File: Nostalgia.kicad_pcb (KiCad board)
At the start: 2 copper layers, 70 x 102 mm, 46 parts, among them J10 490107670612, J20 USB-C6, K85 Val, U30 1117-3.3, U40 ESP32-S3-WROOM-1-N16R8

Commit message: WIP
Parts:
- U40: moved to B.Cu
- turned U40 to 180 degrees

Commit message: WIP
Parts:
- added REF**: TACT_6x6_SMD, _custom:TACT_6x6_SMD, F.Cu at (18.0, -41.2)
- added REF**: TACT_6x6_SMD, _custom:TACT_6x6_SMD, F.Cu at (52.0, -41.2)
- added REF**: TACT_6x6_SMD, _custom:TACT_6x6_SMD, F.Cu at (35.0, -45.2)
- added REF**: TACT_6x6_SMD, _custom:TACT_6x6_SMD, F.Cu at (35.0, -37.2)
- moved K85 81.0 mm to (99.0, -48.0)
- moved K85 59.5 mm to (94.0, -41.0)
- moved K85 57.1 mm to (109.0, -48.0)
- moved K85 44.0 mm to (95.4, -56.0)
- moved K85 5.00 mm to (35.0, -29.0)
- moved K85 5.00 mm to (18.0, -29.0)
- moved K85 5.00 mm to (52.0, -29.0)
- moved K85 4.00 mm to (18.0, -22.0)
- moved K85 4.00 mm to (35.0, -22.0)
- moved K85 4.00 mm to (52.0, -22.0)
- moved K85 3.00 mm to (18.0, -15.0)
- moved K85 3.00 mm to (52.0, -15.0)
- moved K85 3.00 mm to (35.0, -15.0)
- moved K85 2.00 mm to (35.0, -8.00)
- moved K85 2.00 mm to (18.0, -8.00)
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
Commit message: Schemat
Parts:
- removed BT60 (x3): 18650, _custom:Bat_BHC-18650-1P
- removed K85 (x16): Val, _custom:TACT_6x3.5_SMD
- removed the REF** at (18.0, -41.2)
- removed the REF** at (52.0, -41.2)
- removed the REF** at (35.0, -45.2)
- removed the REF** at (35.0, -37.2)
- added BAT1: 18650, _custom:Bat_BH-18650-A1AJ005, B.Cu at (12.0, -38.2)
- added BAT2: 18650, _custom:Bat_BH-18650-A1AJ005, B.Cu at (35.0, -38.2)
- added BAT3: 18650, _custom:Bat_BH-18650-A1AJ005, B.Cu at (58.0, -38.2)
- added C1: 10u, _custom:C_0603, F.Cu at (123.2, -12.3)
- added C2: 10u, _custom:C_0603, F.Cu at (107.6, -7.67)
- added D1: LED, _custom:LED_0805, F.Cu at (108.1, -12.2)
- added D2: LED, _custom:LED_0805, F.Cu at (108.1, -9.85)
- added K1: TACT_6x3_SMD, _custom:TACT_6x3_SMD, F.Cu at (18.0, -29.0)
- added K10: TACT_6x3_SMD, _custom:TACT_6x3_SMD, F.Cu at (18.0, -8.00)
- added K11: TACT_6x3_SMD, _custom:TACT_6x3_SMD, F.Cu at (35.0, -8.00)
- added K12: TACT_6x3_SMD, _custom:TACT_6x3_SMD, F.Cu at (52.0, -8.00)
- added K13: TACT_6x6_SMD, _custom:TACT_6x6_SMD, F.Cu at (18.0, -41.2)
- added K14: TACT_6x6_SMD, _custom:TACT_6x6_SMD, F.Cu at (35.0, -45.2)
- added K15: TACT_6x6_SMD, _custom:TACT_6x6_SMD, F.Cu at (35.0, -37.2)
- added K16: TACT_6x6_SMD, _custom:TACT_6x6_SMD, F.Cu at (52.0, -41.2)
- added K2: TACT_6x3_SMD, _custom:TACT_6x3_SMD, F.Cu at (35.0, -29.0)
- added K3: TACT_6x3_SMD, _custom:TACT_6x3_SMD, F.Cu at (52.0, -29.0)
- added K4: TACT_6x3_SMD, _custom:TACT_6x3_SMD, F.Cu at (18.0, -22.0)
- added K5: TACT_6x3_SMD, _custom:TACT_6x3_SMD, F.Cu at (35.0, -22.0)
- added K6: TACT_6x3_SMD, _custom:TACT_6x3_SMD, F.Cu at (52.0, -22.0)
- added K7: TACT_6x3_SMD, _custom:TACT_6x3_SMD, F.Cu at (18.0, -15.0)
- added K8: TACT_6x3_SMD, _custom:TACT_6x3_SMD, F.Cu at (35.0, -15.2)
- added K9: TACT_6x3_SMD, _custom:TACT_6x3_SMD, F.Cu at (52.0, -15.2)
- added R1: 1k, _custom:R_0603, F.Cu at (123.2, -10.3)
- added R2: 1k, _custom:R_0603, F.Cu at (123.2, -8.38)
- added R3: 1k2, _custom:R_0603, F.Cu at (123.2, -6.42)
- added TP2: Chg, _custom:Testpoint_2.00mm, F.Cu at (117.2, -2.90)
- added TP5: Stby, _custom:Testpoint_2.00mm, F.Cu at (117.2, 0.66)
- added U1: TP4056, _custom:SO8-PowerPad, F.Cu at (118.7, -8.96)
- J10, J20: moved to B.Cu
- moved J20 104.0 mm to (70.0, -82.2)
- moved J10 86.3 mm to (56.5, -99.0), turned to 180 degrees
- moved U40 5.50 mm to (35.4, -95.2)
- moved REF** 2.00 mm to (35.0, -78.0)
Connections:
- J20 pad A9: 5V -> VUSB
- J20 pad B9: 5V -> VUSB
- U40 pad 36: unconnected-(U40-Rx0/IO44-Pad36) -> /Debug-Rx
- U40 pad 37: unconnected-(U40-Tx0/IO43-Pad37) -> /Debug-Tx

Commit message: WIP
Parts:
- added C10: 100n, _custom:C_0603, F.Cu at (125.7, 3.37)
- added C4: 10u, _custom:C_0603, F.Cu at (125.7, -0.53)
- added C5: 10u, _custom:C_0603, F.Cu at (125.7, 1.42)
- added U5: TPS613222ADBV, _custom:SOT23-5, F.Cu at (129.3, 0.56)

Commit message: WIP
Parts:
- removed C30, C32: 10u, _custom:C_0603
- removed C31, C33: 1u, _custom:C_0603
- removed FID1, FID2, FID3, FID4, FID5, FID6: 1.00mm, _custom:Fiducial_1.00mm
- removed REF**: OLED_2.42inch_board, _custom:OLED_2.42inch_board
- removed TP2: Chg, _custom:Testpoint_2.00mm
- removed TP5: Stby, _custom:Testpoint_2.00mm
- removed U30: 1117-3.3, _custom:SOT223
- added C3: 10u, _custom:C_0603, F.Cu at (60.6, 9.25)
- added C6: 10u, _custom:C_0603, F.Cu at (60.6, 11.2)
- added C7: 100n, _custom:C_0603, F.Cu at (60.6, 13.2)
- added C8: 10u, _custom:C_0603, F.Cu at (60.6, 15.1)
- added DISP1: OLED, _custom:OLED_2.42inch_board, F.Cu at (35.0, -78.0)
- added L1: 2.2uH, _custom:DJNR3015, F.Cu at (73.5, 12.2)
- added L4: 4.7uH, _custom:DJNR3015, F.Cu at (125.8, 6.50)
- added R4: 1M, _custom:R_0603, F.Cu at (60.6, 17.1)
- added R5: 180k, _custom:R_0603, F.Cu at (60.6, 19.0)
- added R6: 100R, _custom:R_0603, F.Cu at (60.6, 20.9)
- added U2: TPS63000, _custom:Texas_DRC0010J_ThermalVias, F.Cu at (73.3, 17.8)
- C10: value 100n -> 10u
- moved J10 41.4 mm to (15.1, -98.7)
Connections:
- J10 pad 2: 5V -> VUSB
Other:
- board text added: "102"
- board text removed: "70"

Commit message: WIP
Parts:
- removed DISP1: OLED, _custom:OLED_2.42inch_board
- added DISP2: OLED, _custom:OLED_2.42inch_board_2, F.Cu at (35.5, -80.2)
- added R7: 1M, _custom:R_0603, F.Cu at (89.2, 1.00)
- K1, K10, K11, K12, K2, K3, K4, K5, K6, K7, K8, K9: value TACT_6x3_SMD -> CONFIG
- moved BAT1 0.50 mm to (12.5, -38.2)
- moved BAT2 0.50 mm to (35.5, -38.2)
- moved BAT3 0.50 mm to (58.5, -38.2)
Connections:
- K1 pad 1: unconnected-(K1-Pad1) -> /Col0
- K1 pad 2: unconnected-(K1-Pad2) -> /Row0
- K10 pad 1: unconnected-(K10-Pad1) -> /Col0
- K10 pad 2: unconnected-(K10-Pad2) -> /Row3
- K11 pad 1: unconnected-(K11-Pad1) -> /Col1
- K11 pad 2: unconnected-(K11-Pad2) -> /Row3
- K12 pad 1: unconnected-(K12-Pad1) -> /Col2
- K12 pad 2: unconnected-(K12-Pad2) -> /Row3
- K13 pad 1: unconnected-(K13-Pad1) -> /Col3
- K13 pad 2: unconnected-(K13-Pad2) -> /Row2
- K14 pad 1: unconnected-(K14-Pad1) -> /Col3
- K14 pad 2: unconnected-(K14-Pad2) -> /Row0
- K15 pad 1: unconnected-(K15-Pad1) -> /Col3
- K15 pad 2: unconnected-(K15-Pad2) -> /Row1
- K16 pad 1: unconnected-(K16-Pad1) -> /Col3
- K16 pad 2: unconnected-(K16-Pad2) -> /Row3
- K2 pad 1: unconnected-(K2-Pad1) -> /Col1
- K2 pad 2: unconnected-(K2-Pad2) -> /Row0
- K3 pad 1: unconnected-(K3-Pad1) -> /Col2
- K3 pad 2: unconnected-(K3-Pad2) -> /Row0
- K4 pad 1: unconnected-(K4-Pad1) -> /Col0
- K4 pad 2: unconnected-(K4-Pad2) -> /Row1
- K5 pad 1: unconnected-(K5-Pad1) -> /Col1
- K5 pad 2: unconnected-(K5-Pad2) -> /Row1
- K6 pad 1: unconnected-(K6-Pad1) -> /Col2
- K6 pad 2: unconnected-(K6-Pad2) -> /Row1
- K7 pad 1: unconnected-(K7-Pad1) -> /Col0
- K7 pad 2: unconnected-(K7-Pad2) -> /Row2
- K8 pad 1: unconnected-(K8-Pad1) -> /Col1
- K8 pad 2: unconnected-(K8-Pad2) -> /Row2
- K9 pad 1: unconnected-(K9-Pad1) -> /Col2
- K9 pad 2: unconnected-(K9-Pad2) -> /Row2
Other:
- board size 70 x 102 mm -> 71 x 102 mm

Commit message: WIP
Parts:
- moved K16 7.94 mm to (59.0, -45.0)
- moved K12 7.62 mm to (59.0, -11.0)
- moved K3 7.62 mm to (59.0, -32.0)
- moved K6 7.62 mm to (59.0, -25.0)
- moved K9 7.62 mm to (59.0, -18.2)
- moved K13 6.25 mm to (13.0, -45.0)
- moved K1 5.83 mm to (13.0, -32.0)
- moved K10 5.83 mm to (13.0, -11.0)
- moved K4 5.83 mm to (13.0, -25.0)
- moved K7 5.83 mm to (13.0, -18.0)
- moved K14 3.88 mm to (36.0, -49.0)
- moved K15 3.88 mm to (36.0, -41.0)
- moved K11 3.16 mm to (36.0, -11.0)
- moved K2 3.16 mm to (36.0, -32.0)
- moved K5 3.16 mm to (36.0, -25.0)
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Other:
- board size 71 x 102 mm -> 72 x 102 mm
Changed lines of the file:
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@@
 	(footprint "_custom:TACT_6x3_SMD"
 		(layer "F.Cu")
-		(at 35 -8)
+		(at 36 -11)
 		(descr "SMD Pushbutton")
 		(property "Reference" "K11"
@@
 	(footprint "_custom:TACT_6x3_SMD"
 		(layer "F.Cu")
-		(at 52 -22)
+		(at 59 -25)
 		(descr "SMD Pushbutton")
 		(property "Reference" "K6"
@@
 	(footprint "_custom:TACT_6x3_SMD"
 		(layer "F.Cu")
-		(at 35 -15.25)
+		(at 36 -18.25)
 		(descr "SMD Pushbutton")
 		(property "Reference" "K8"
@@
 	(footprint "_custom:TACT_6x6_SMD"
 		(layer "F.Cu")
-		(at 35 -45.25 180)
+		(at 36 -49 180)
 		(descr "C&K Components SPST SMD PTS645 Series 6mm Tact Switch")
 		(tags "SPST Button Switch")
@@
 	(footprint "_custom:TACT_6x3_SMD"
 		(layer "F.Cu")
-		(at 18 -8)
+		(at 13 -11)
 		(descr "SMD Pushbutton")
 		(property "Reference" "K10"
@@
 	(footprint "_custom:TACT_6x3_SMD"
 		(layer "F.Cu")
-		(at 35 -22)
+		(at 36 -25)
 		(descr "SMD Pushbutton")
 		(property "Reference" "K5"
@@
 	(footprint "_custom:TACT_6x3_SMD"
 		(layer "F.Cu")
-		(at 18 -15)
+		(at 13 -18)
 		(descr "SMD Pushbutton")
 		(property "Reference" "K7"
@@
 	(footprint "_custom:TACT_6x6_SMD"
 		(layer "F.Cu")
-		(at 52 -41.25)
+		(at 59 -45)
 		(descr "C&K Components SPST SMD PTS645 Series 6mm Tact Switch")
 		(tags "SPST Button Switch")
@@
 	(footprint "_custom:TACT_6x6_SMD"
 		(layer "F.Cu")
-		(at 35 -37.25)
+		(at 36 -41)
 		(descr "C&K Components SPST SMD PTS645 Series 6mm Tact Switch")
 		(tags "SPST Button Switch")
@@
 	(footprint "_custom:TACT_6x3_SMD"
 		(layer "F.Cu")
-		(at 18 -22)
+		(at 13 -25)
 		(descr "SMD Pushbutton")
 		(property "Reference" "K4"
@@
 	(footprint "_custom:OLED_2.42inch_board_2"
 		(layer "F.Cu")
-		(at 35.5 -80.25)
+		(at 36 -80.25)
 		(property "Reference" "DISP2"
 			(at 0 -0.5 0)
@@
 		)
 		(fp_line
-			(start -31 -19.5)
-			(end -31 19.5)
+			(start -31 -18.8)
+			(end -31 20.2)
 			(stroke
 				(width 0.1)
@@
 		)
 		(fp_line
-			(start -19 19.5)
-			(end -31 19.5)
+			(start -19 20.2)
+			(end -31 20.2)
 			(stroke
 				(width 0.1)
@@
 		)
 		(fp_line
-			(start -19 19.5)
-			(end -18 20.5)
+			(start -19 20.2)
+			(end -18 21.2)
 			(stroke
 				(width 0.1)
@@
 		)
 		(fp_line
-			(start -18 20.5)
-			(end 18 20.5)
+			(start -18 21.2)
+			(end 18 21.2)
 			(stroke
 				(width 0.1)
@@
 		)
 		(fp_line
-			(start 19 19.5)
-			(end 18 20.5)
+			(start 19 20.2)
+			(end 18 21.2)
 			(stroke
 				(width 0.1)
@@
 		)
 		(fp_line
-			(start 31 -19.5)
-			(end -31 -19.5)
+			(start 31 -18.8)
+			(end -31 -18.8)
 			(stroke
 				(width 0.1)
@@
 		)
 		(fp_line
-			(start 31 19.5)
-			(end 19 19.5)
+			(start 31 20.2)
+			(end 19 20.2)
 			(stroke
 				(width 0.1)
@@
 		)
 		(fp_line
-			(start 31 19.5)
-			(end 31 -19.5)
+			(start 31 20.2)
+			(end 31 -18.8)
 			(stroke
 				(width 0.1)
@@
 		)
 		(fp_rect
-			(start -28.75 -17.5)
-			(end 28.75 12)
+			(start -28.75 -16.8)
+			(end 28.75 12.7)
 			(stroke
 				(width 0.1)
@@
 		)
 		(pad "1" thru_hole circle
-			(at -32.5 -21.5)
+			(at -33.5 -19.75)
 			(size 4 4)
-			(drill 3)
+			(drill 2.5)
 			(layers "*.Cu" "*.Mask")
 			(remove_unused_layers no)
@@
 		)
 		(pad "1" thru_hole circle
-			(at -32.5 21.25)
+			(at -33.5 19.75)
 			(size 4 4)
-			(drill 3)
+			(drill 2.5)
 			(layers "*.Cu" "*.Mask")
 			(remove_unused_layers no)
@@
 		)
 		(pad "1" thru_hole oval
-			(at 7.62 -20.5 90)
+			(at 7.62 -20.3 90)
 			(size 2.8 1.8)
 			(drill 1)
@@
 		)
 		(pad "1" thru_hole circle
-			(at 32.5 -21.25)
+			(at 33.5 -19.75)
 			(size 4 4)
-			(drill 3)
+			(drill 2.5)
 			(layers "*.Cu" "*.Mask")
 			(remove_unused_layers no)
@@
 		)
 		(pad "1" thru_hole circle
-			(at 32.5 21.25)
+			(at 33.5 19.75)
 			(size 4 4)
-			(drill 3)
+			(drill 2.5)
 			(layers "*.Cu" "*.Mask")
 			(remove_unused_layers no)
@@
 		)
 		(pad "2" thru_hole oval
-			(at 5.08 -20.5 90)
+			(at 5.08 -20.3 90)
 			(size 2.8 1.8)
 			(drill 1)
@@
 		)
 		(pad "3" thru_hole oval
-			(at 2.54 -20.5 90)
+			(at 2.54 -20.3 90)
 			(size 2.8 1.8)
 			(drill 1)
@@
 		)
 		(pad "4" thru_hole oval
-			(at 0 -20.5 90)
+			(at 0 -20.3 90)
 			(size 2.8 1.8)
 			(drill 1)
@@
 		)
 		(pad "5" thru_hole oval
-			(at -2.54 -20.5 90)
+			(at -2.54 -20.3 90)
 			(size 2.8 1.8)
 			(drill 1)
@@
 		)
 		(pad "6" thru_hole oval
-			(at -5.08 -20.5 90)
+			(at -5.08 -20.3 90)
 			(size 2.8 1.8)
 			(drill 1)
@@
 		)
 		(pad "7" thru_hole oval
-			(at -7.62 -20.5 90)
+			(at -7.62 -20.3 90)
 			(size 2.8 1.8)
 			(drill 1)
@@
 	(footprint "_custom:TACT_6x3_SMD"
 		(layer "F.Cu")
-		(at 18 -29)
+		(at 13 -32)
 		(descr "SMD Pushbutton")
 		(property "Reference" "K1"
@@
 	(footprint "_custom:TACT_6x3_SMD"
 		(layer "F.Cu")
-		(at 52 -29)
+		(at 59 -32)
 		(descr "SMD Pushbutton")
 		(property "Reference" "K3"
@@
 	(footprint "_custom:TACT_6x3_SMD"
 		(layer "F.Cu")
-		(at 35 -29)
+		(at 36 -32)
 		(descr "SMD Pushbutton")
 		(property "Reference" "K2"
@@
 	(footprint "_custom:TACT_6x3_SMD"
 		(layer "F.Cu")
-		(at 52 -15.25)
+		(at 59 -18.25)
 		(descr "SMD Pushbutton")
 		(property "Reference" "K9"
@@
 	(footprint "_custom:TACT_6x3_SMD"
 		(layer "F.Cu")
-		(at 52 -8)
+		(at 59 -11)
 		(descr "SMD Pushbutton")
 		(property "Reference" "K12"
@@
 	(footprint "_custom:TACT_6x6_SMD"
 		(layer "F.Cu")
-		(at 18 -41.25)
+		(at 13 -45)
 		(descr "C&K Components SPST SMD PTS645 Series 6mm Tact Switch")
 		(tags "SPST Button Switch")
@@
 	(footprint "_custom:Bat_BH-18650-A1AJ005"
 		(layer "B.Cu")
-		(at 35.5 -38.25 90)
+		(at 36 -38.25 90)
 		(property "Reference" "BAT2"
 			(at 39 0 0)
@@
 	(footprint "_custom:Bat_BH-18650-A1AJ005"
 		(layer "B.Cu")
-		(at 12.5 -38.25 90)
+		(at 13 -38.25 90)
 		(property "Reference" "BAT1"
 			(at 39 0 0)
@@
 	(footprint "_custom:Bat_BH-18650-A1AJ005"
 		(layer "B.Cu")
-		(at 58.5 -38.25 90)
+		(at 59 -38.25 90)
 		(property "Reference" "BAT3"
 			(at 39 0 0)
@@
 	(gr_line
 		(start 0 0)
-		(end 71 0)
+		(end 72 0)
 		(stroke
 			(width 0.1)
@@
 	)
 	(gr_line
-		(start 71 0)
-		(end 71 -102)
+		(start 72 0)
+		(end 72 -102)
 		(stroke
 			(width 0.1)
@@
 	)
 	(gr_line
-		(start 71 -102)
+		(start 72 -102)
 		(end 0 -102)
 		(stroke

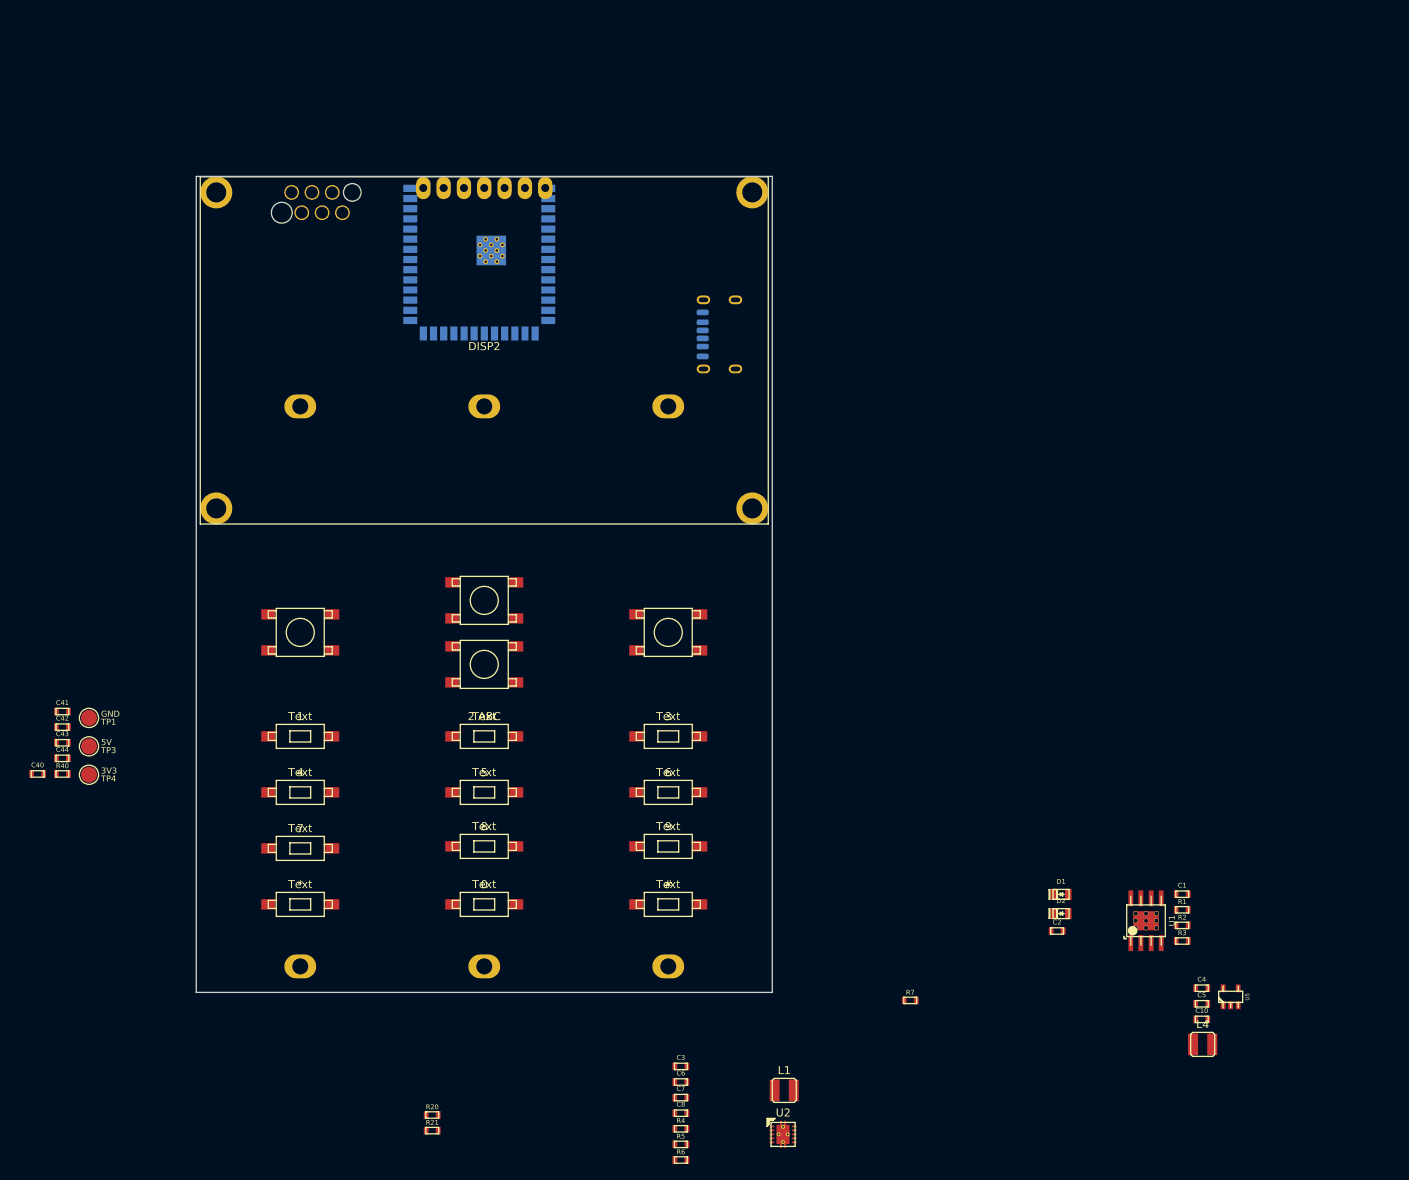
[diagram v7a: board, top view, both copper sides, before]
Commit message: Wydłużenie płytki i zmiana przycisków z 6x3 na 6x6
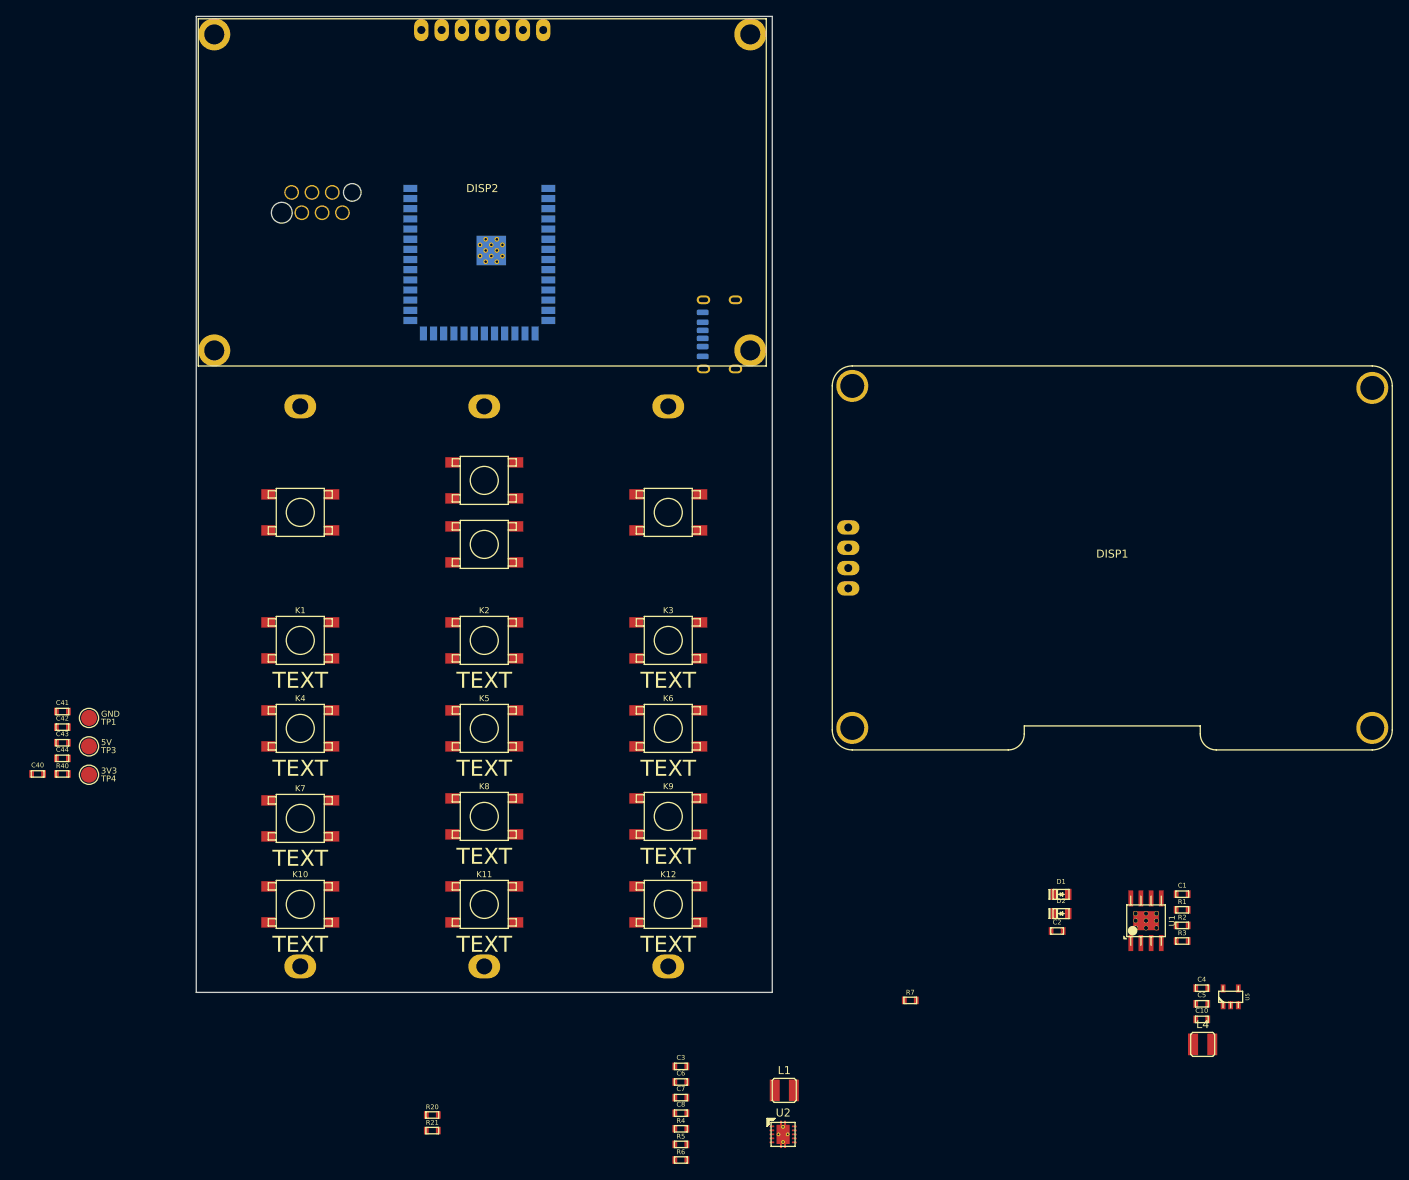
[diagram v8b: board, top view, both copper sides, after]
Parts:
- added DISP1: OLED, _custom:OLED_2.42inch_board, F.Cu at (114.5, -54.3)
- K1, K10, K11, K12, K2, K3, K4, K5, K6, K7, K8, K9: value CONFIG -> TACT_6x3_SMD; footprint _custom:TACT_6x3_SMD -> _custom:TACT_6x6_SMD
- moved DISP2 19.8 mm to (35.8, -100.0)
- moved K13 15.0 mm to (13.0, -60.0)
- moved K14 15.0 mm to (36.0, -64.0)
- moved K15 15.0 mm to (36.0, -56.0)
- moved K16 15.0 mm to (59.0, -60.0)
- moved K1 12.0 mm to (13.0, -44.0)
- moved K2 12.0 mm to (36.0, -44.0)
- moved K3 12.0 mm to (59.0, -44.0)
- moved K4 8.00 mm to (13.0, -33.0)
- moved K5 8.00 mm to (36.0, -33.0)
- moved K6 8.00 mm to (59.0, -33.0)
- moved K7 3.75 mm to (13.0, -21.8)
- moved K8 3.75 mm to (36.0, -22.0)
- moved K9 3.75 mm to (59.0, -22.0)
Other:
- board size 72 x 102 mm -> 72 x 122 mm
